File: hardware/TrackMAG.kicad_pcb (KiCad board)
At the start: 2 copper layers, 48 parts, among them J1 USB_C_Socket_USB2.0, J2 Conn_Debug, SW1 SW_RESET, SW2 SW_BOOT0, U1 LSM6DS3TR-C, U2 USBLC6-2P6, U3 STM32F103C8T6, U4 LIS2MDLTR, U5 AMS1117-3.3, Y1 16MHz

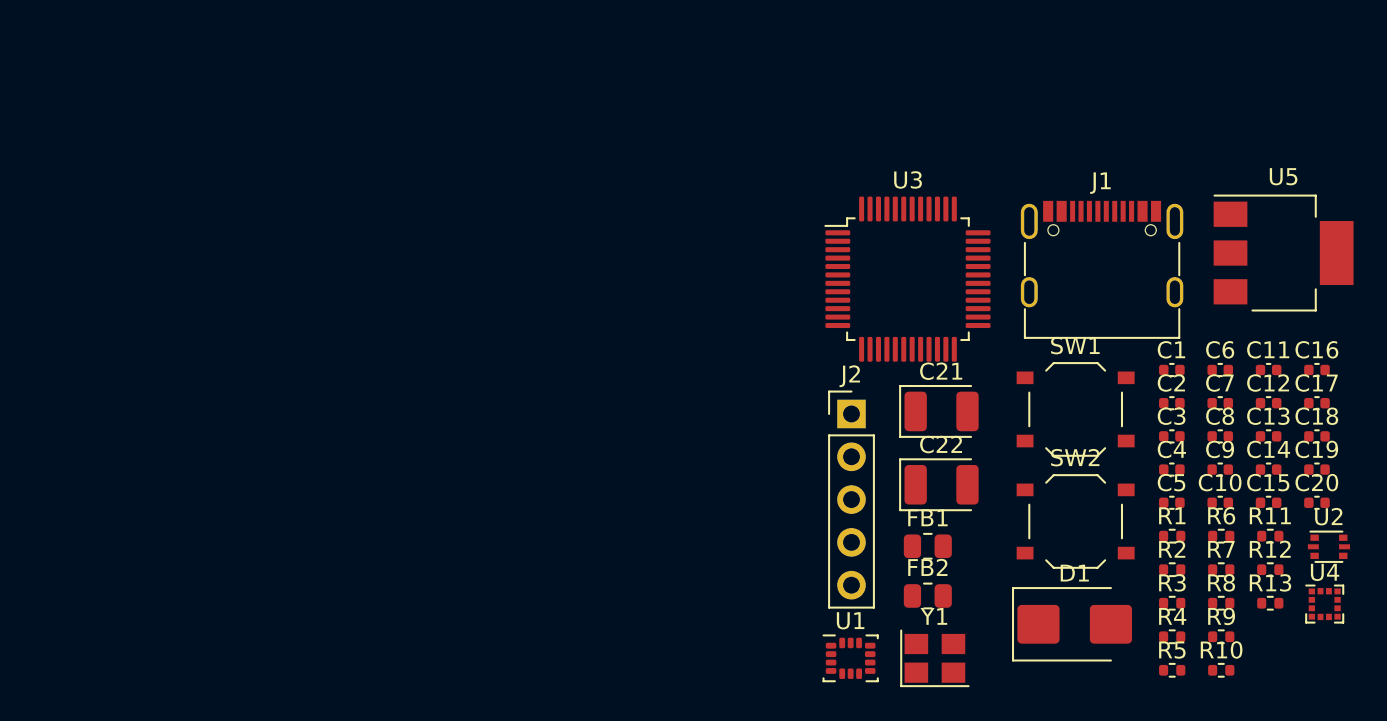
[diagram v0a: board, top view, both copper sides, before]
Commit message: Update pinout to match current firmware configuration
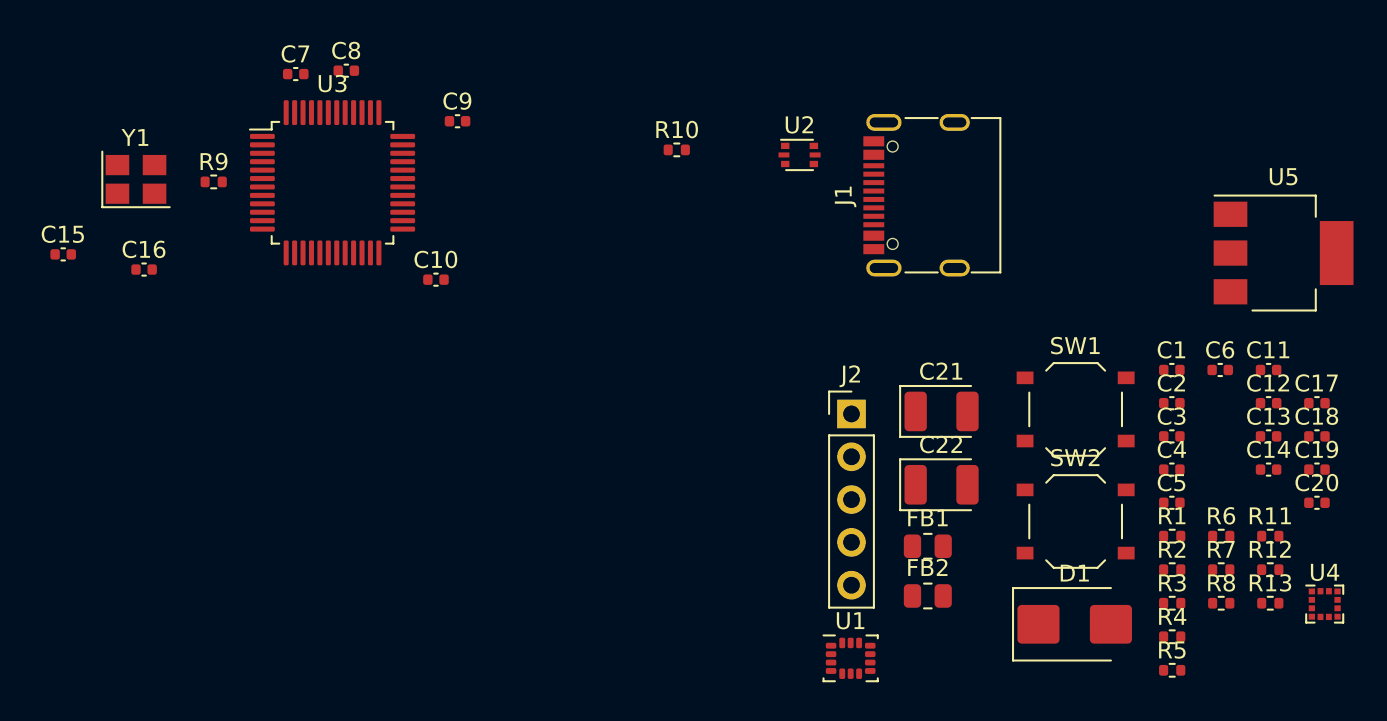
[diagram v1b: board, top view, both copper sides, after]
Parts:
- moved C15 73.0 mm to (82.3, 74.6)
- moved C16 69.9 mm to (87.1, 75.5)
- moved R9 65.6 mm to (91.2, 70.3)
- moved C7 58.2 mm to (96.1, 63.9)
- moved C8 56.2 mm to (99.1, 63.7)
- moved Y1 55.3 mm to (86.6, 70.2)
- moved C9 49.8 mm to (105.7, 66.7)
- moved C10 48.4 mm to (104.4, 76.1)
- moved R10 44.7 mm to (118.7, 68.4)
- moved U2 39.1 mm to (126.0, 68.7)
- moved U3 34.6 mm to (98.3, 70.3)
- moved J1 10.9 mm to (134.1, 71.1), turned to 90 degrees
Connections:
- U3 pad 18: INT1 -> unconnected-(U3-PB0-Pad18)
- U3 pad 39: TRACESWO -> unconnected-(U3-PB3-Pad39)
- U3 pad 40: unconnected-(U3-PB4-Pad40) -> TRACESWO
- U3 pad 41: DRDY -> unconnected-(U3-PB5-Pad41)
- U3 pad 45: unconnected-(U3-PB8-Pad45) -> DRDY
- U3 pad 46: unconnected-(U3-PB9-Pad46) -> INT1
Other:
- copper layers 2 -> 4

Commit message: Backup current progress
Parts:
- removed the C18 at (156.7, 85.4)
- removed the C19 at (156.7, 87.4)
- removed C20: 1u, Capacitor_SMD:C_0402_1005Metric
- removed FB2: 100R, Resistor_SMD:R_0805_2012Metric
- added D1: LED, LED_SMD:LED_0603_1608Metric, F.Cu at (90.9, 65.5)
- added H1: MountingHole, MountingHole:MountingHole_2.1mm, F.Cu at (40.8, 35.0)
- added H2: MountingHole, MountingHole:MountingHole_2.1mm, F.Cu at (70.8, 35.0)
- added H3: MountingHole, MountingHole:MountingHole_2.1mm, F.Cu at (70.8, 65.0)
- BOOT: renamed from SW2; footprint Button_Switch_SMD:SW_Push_1P1T_XKB_TS-1187A -> TrackMAG:SW_Push_1P1T_XKB_TS-1187A
- C1, C10, C11, C12, C13, C14, C15, C16, C17, C2, C3, C4, C5, C6, C7, C8, C9: footprint Capacitor_SMD:C_0402_1005Metric -> TrackMAG:C_0402_1005Metric
- J1: footprint Connector_USB:USB_C_Receptacle_G-Switch_GT-USB-7010ASV -> TrackMAG:USB_C_Receptacle_G-Switch_GT-USB-7010ASV
- J2: footprint Connector_PinHeader_2.54mm:PinHeader_1x05_P2.54mm_Vertical -> TrackMAG:PinHeader_1x05_P2.54mm_Debug
- R1, R10, R11, R12, R2, R3, R4, R5, R6: footprint Resistor_SMD:R_0402_1005Metric -> TrackMAG:R_0402_1005Metric
- R13: value 0 -> 1k5; footprint Resistor_SMD:R_0402_1005Metric -> TrackMAG:R_0402_1005Metric
- R7: renamed from R8; footprint Resistor_SMD:R_0402_1005Metric -> TrackMAG:R_0402_1005Metric
- R8: renamed from R9; footprint Resistor_SMD:R_0402_1005Metric -> TrackMAG:R_0402_1005Metric
- R9: renamed from R7; footprint Resistor_SMD:R_0402_1005Metric -> TrackMAG:R_0402_1005Metric
- RESET: renamed from SW1; footprint Button_Switch_SMD:SW_Push_1P1T_XKB_TS-1187A -> TrackMAG:SW_Push_1P1T_XKB_TS-1187A
- U1: footprint Package_LGA:LGA-14_3x2.5mm_P0.5mm_LayoutBorder3x4y -> TrackMAG:LGA-14_3x2.5mm_P0.5mm_LayoutBorder3x4y
- U2: footprint Package_TO_SOT_SMD:SOT-666 -> TrackMAG:SOT-666
- U4: value LIS2MDLTR -> LIS2MDL; footprint Package_LGA:LGA-12_2x2mm_P0.5mm -> TrackMAG:LGA-12_2x2mm_P0.5mm
- moved C13 110.0 mm to (47.5, 57.1), turned to 180 degrees
- moved C12 109.9 mm to (47.5, 55.6), turned to 180 degrees
- moved BOOT 109.8 mm to (43.9, 41.7), turned to 180 degrees
- moved C11 109.8 mm to (48.2, 51.5), turned to 90 degrees
- moved C6 107.5 mm to (49.6, 45.5), turned to -90 degrees
- moved U5 101.2 mm to (59.5, 40.2), turned to 180 degrees
- moved U4 100.8 mm to (61.6, 63.2), turned to 90 degrees
- moved R6 97.4 mm to (64.3, 46.8), turned to -90 degrees
- moved R5 96.1 mm to (64.3, 52.2), turned to 90 degrees
- moved C19 95.2 mm to (52.2, 40.2), turned to 180 degrees
- moved D2 93.0 mm to (68.3, 40.2)
- moved FB1 91.2 mm to (49.5, 56.4), turned to -90 degrees
- moved RESET 90.8 mm to (54.1, 62.2), turned to 180 degrees
- moved J2 90.1 mm to (41.0, 65.2), turned to 180 degrees
- moved C18 89.6 mm to (59.5, 34.7), turned to 180 degrees
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- renumbered C21 to C18, C22 to C19, D1 to D2
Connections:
- net Net-(J1-CC1) renamed /CC1
- net Net-(J1-CC2) renamed /CC2
- net Net-(U1-INT2) renamed /INT2
- net Net-(U4-C1) renamed /C1
- C16 pad 1: Net-(C16-Pad1) -> /HSE_OUT
- C19 pad 1: Net-(U5-VO) -> +3.3V
- J1 pad A6: Net-(J1-D+-PadA6) -> /US_D+
- J1 pad A7: Net-(J1-D--PadA7) -> /US_D-
- J1 pad B6: Net-(J1-D+-PadA6) -> /US_D+
- J1 pad B7: Net-(J1-D--PadA7) -> /US_D-
- J1 pad S1: Net-(J1-SHIELD) -> GND
- R13 pad 1: GND -> Net-(D1-K)
- R13 pad 2: Net-(J1-SHIELD) -> GND
- R3 pad 1: I2C1_SDA -> I2C2_SDA
- R8 pad 1: Net-(C16-Pad1) -> /HSE_OUT
- R8 pad 2: /HSE_OUT -> /HSE_O
- U1 pad 13: I2C1_SCL -> I2C2_SCL
- U1 pad 14: I2C1_SDA -> I2C2_SDA
- U2 pad 1: /USB_D+ -> /US_D+
- U2 pad 3: Net-(J1-D+-PadA6) -> /USB_D+
- U2 pad 4: Net-(J1-D--PadA7) -> /USB_D-
- U2 pad 6: /USB_D- -> /US_D-
- U3 pad 21: unconnected-(U3-PB10-Pad21) -> I2C2_SCL
- U3 pad 22: unconnected-(U3-PB11-Pad22) -> I2C2_SDA
- U3 pad 42: I2C1_SCL -> unconnected-(U3-PB6-Pad42)
- U3 pad 43: I2C1_SDA -> unconnected-(U3-PB7-Pad43)
- U3 pad 6: /HSE_OUT -> /HSE_O
- U5 pad 2: Net-(U5-VO) -> +3.3V
- Y1 pad 3: Net-(C16-Pad1) -> /HSE_OUT
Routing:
- net /HSE_IN: track 0.00 -> 9.64 mm
- net /US_D+: track 0.00 -> 5.12 mm
- net /USB_D+: track 0.00 -> 5.11 mm
- net /USB_D-: track 0.00 -> 5.11 mm
- net /US_D-: track 0.00 -> 4.27 mm
- net /HSE_OUT: track 0.00 -> 3.31 mm
- net /HSE_O: track 0.00 -> 3.08 mm
- added copper zone on B.Cu, net GND
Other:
- board outline added: 36 x 36 mm

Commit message: Backup currend KiCAD progress
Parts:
- removed the C5 at (120.4, 61.0)
- removed R9: 0, TrackMAG:R_0402_1005Metric
- added C1: 1u, TrackMAG:C_0402_1005Metric, F.Cu at (64.7, 56.2)
- added C18: 10u, Capacitor_Tantalum_SMD:CP_EIA-3216-18_Kemet-A, F.Cu at (70.9, 43.2)
- added C19: 100n, TrackMAG:C_0402_1005Metric, F.Cu at (67.6, 43.3)
- added C2: 1u, TrackMAG:C_0402_1005Metric, F.Cu at (63.6, 56.2)
- added C20: 10n, TrackMAG:C_0402_1005Metric, F.Cu at (66.2, 43.3)
- added C3: 1u, TrackMAG:C_0402_1005Metric, F.Cu at (62.5, 56.2)
- added C8: 10u, Capacitor_Tantalum_SMD:CP_EIA-3216-18_Kemet-A, F.Cu at (67.7, 56.6)
- added FB2: 100R, Resistor_SMD:R_0805_2012Metric, F.Cu at (64.3, 43.8)
- SW1: renamed from RESET; footprint TrackMAG:SW_Push_1P1T_XKB_TS-1187A -> TrackMAG:SW_Push_1P1T_XKB_TS-1187A_RESET
- SW2: renamed from BOOT; value SW_BOOT0 -> SW_BOOT; footprint TrackMAG:SW_Push_1P1T_XKB_TS-1187A -> TrackMAG:SW_Push_1P1T_XKB_TS-1187A_BOOT
- moved R1 63.6 mm to (47.0, 44.1)
- moved C17 62.9 mm to (47.0, 45.4)
- moved R7 62.7 mm to (50.0, 59.6)
- moved R2 56.4 mm to (54.2, 57.6), turned to 180 degrees
- moved C5 52.8 mm to (63.6, 57.8), turned to 180 degrees
- moved R4 51.1 mm to (62.2, 63.1), turned to -90 degrees
- moved R3 48.2 mm to (56.6, 57.6)
- moved R11 46.9 mm to (67.9, 63.0), turned to -90 degrees
- moved R12 46.0 mm to (66.4, 63.0), turned to -90 degrees
- moved R13 43.6 mm to (71.0, 35.1), turned to -90 degrees
- moved H2 42.4 mm to (40.8, 65.0)
- moved C23 40.4 mm to (69.1, 60.3), turned to 90 degrees
- moved D1 38.2 mm to (68.6, 34.6), turned to 180 degrees
- moved C4 35.7 mm to (65.2, 60.2), turned to 90 degrees
- moved C6 33.7 mm to (67.5, 58.3)
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- renumbered C7 to C10, C8 to C11, C9 to C12, C10 to C13, C11 to C14, C12 to C15, C13 to C16, C14 to C17, C15 to C21, C16 to C22, C17 to C23, C18 to C24, C19 to C25, C1 to C4, C2 to C5, C3 to C6, C4 to C7, C6 to C9
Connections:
- C24 pad 1: VBUS -> +5V
- D2 pad 1: VBUS -> +5V
- J2 pad 1: /SWDIO -> RESET
- J2 pad 2: /SWCLK -> SWO
- J2 pad 3: TRACESWO -> /SWCLK
- J2 pad 4: RESET -> GND
- J2 pad 5: GND -> /SWDIO
- R2 pad 1: I2C_SCX -> I2C2_SCL
- U1 pad 9: /INT2 -> GND
- U2 pad 1: /US_D+ -> /USB_D-
- U2 pad 3: /USB_D+ -> /US_D-
- U2 pad 4: /USB_D- -> /US_D+
- U2 pad 5: VBUS -> +5V
- U2 pad 6: /US_D- -> /USB_D+
- U3 pad 16: unconnected-(U3-PA6-Pad16) -> INT1
- U3 pad 40: TRACESWO -> SWO
- U3 pad 46: INT1 -> unconnected-(U3-PB9-Pad46)
- U5 pad 3: VBUS -> +5V
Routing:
- net +3.3V: track 0.00 -> 120.2 mm, vias 0 -> 8
- net GND: track 0.00 -> 112.0 mm, vias 0 -> 18
- net RESET: track 0.00 -> 65.3 mm
- net DRDY: track 0.00 -> 29.9 mm, vias 0 -> 2
- net INT1: track 0.00 -> 23.3 mm, vias 0 -> 2
- net /BOOT0: track 0.00 -> 22.6 mm
- net /SWDIO: track 0.00 -> 19.9 mm
- net VBUS: track 0.00 -> 17.6 mm
- net /SWCLK: track 0.00 -> 16.6 mm
- net SWO: track 0.00 -> 16.4 mm
- net I2C2_SCL: track 0.00 -> 12.0 mm, vias 0 -> 2
- net I2C2_SDA: track 0.00 -> 11.2 mm
- net I2C_SDX: track 0.00 -> 7.66 mm
- net +3.3VA: track 0.00 -> 7.08 mm
- net +5V: track 0.00 -> 5.53 mm
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- added copper zone on F.Cu, net +3.3V
- added copper zone on F.Cu, net +5V
- added copper zone on F.Cu, net GND
